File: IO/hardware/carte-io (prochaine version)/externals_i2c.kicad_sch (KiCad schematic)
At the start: 42 parts, among them J10 114020164, J11 114020164, J12 114020164, J13 114020164, J14 114020164, J15 114020164, J16 114020164, J17 114020164, J23 114020164, J24 114020164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

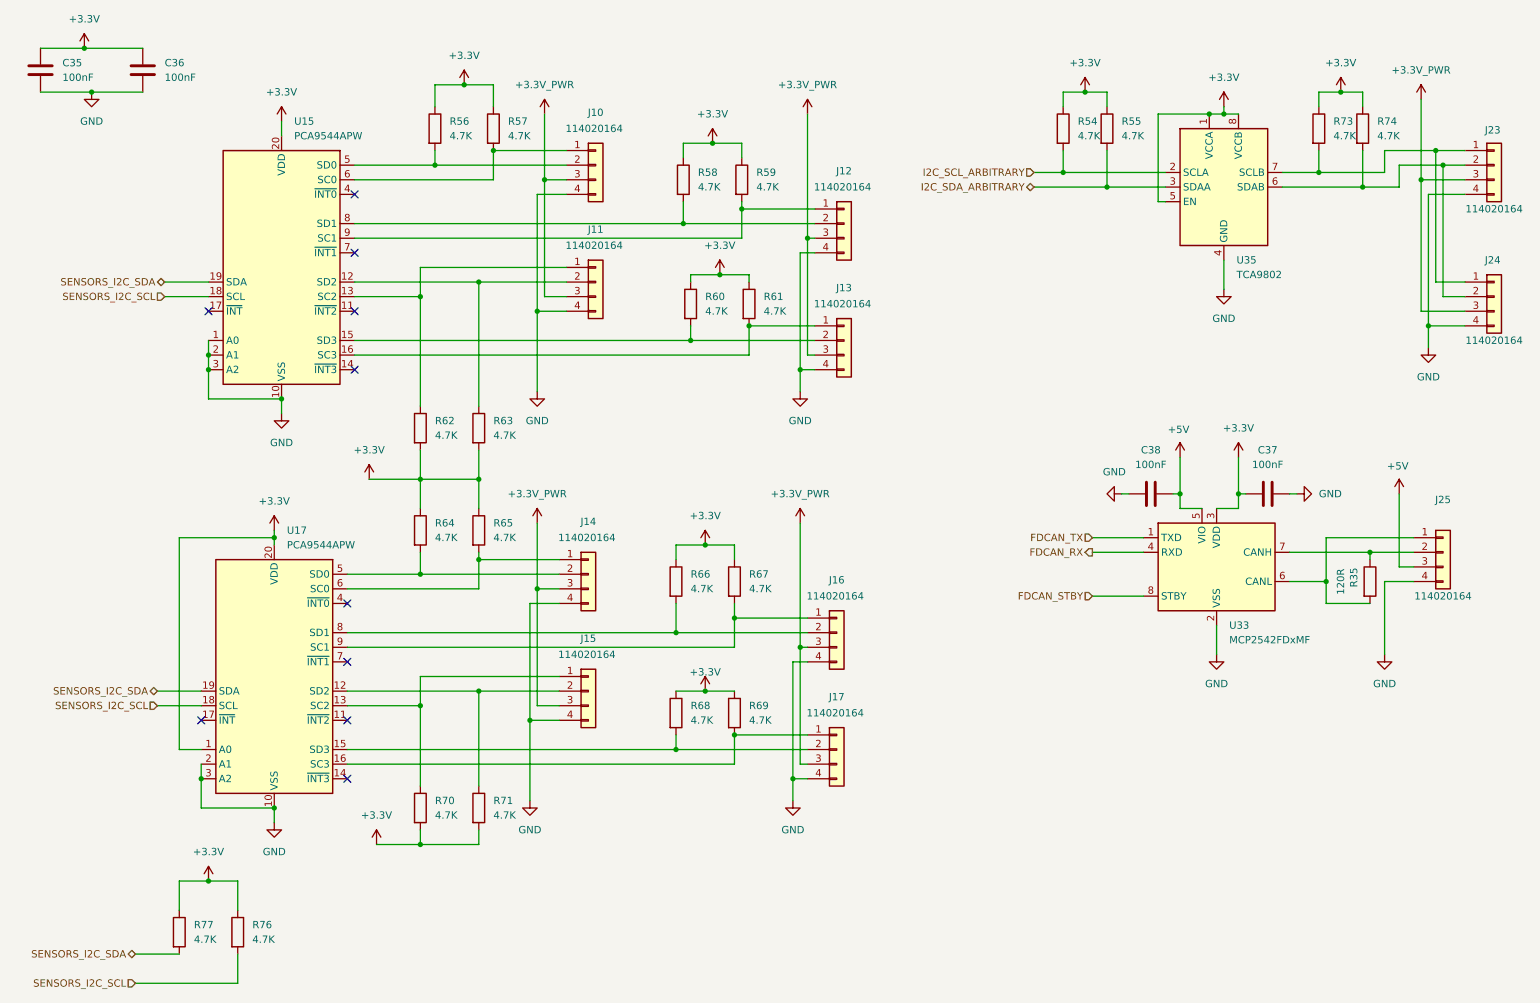
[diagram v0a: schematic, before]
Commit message: Recuperation de la carte IO perdue lors de la suppression des 3 derniers commit
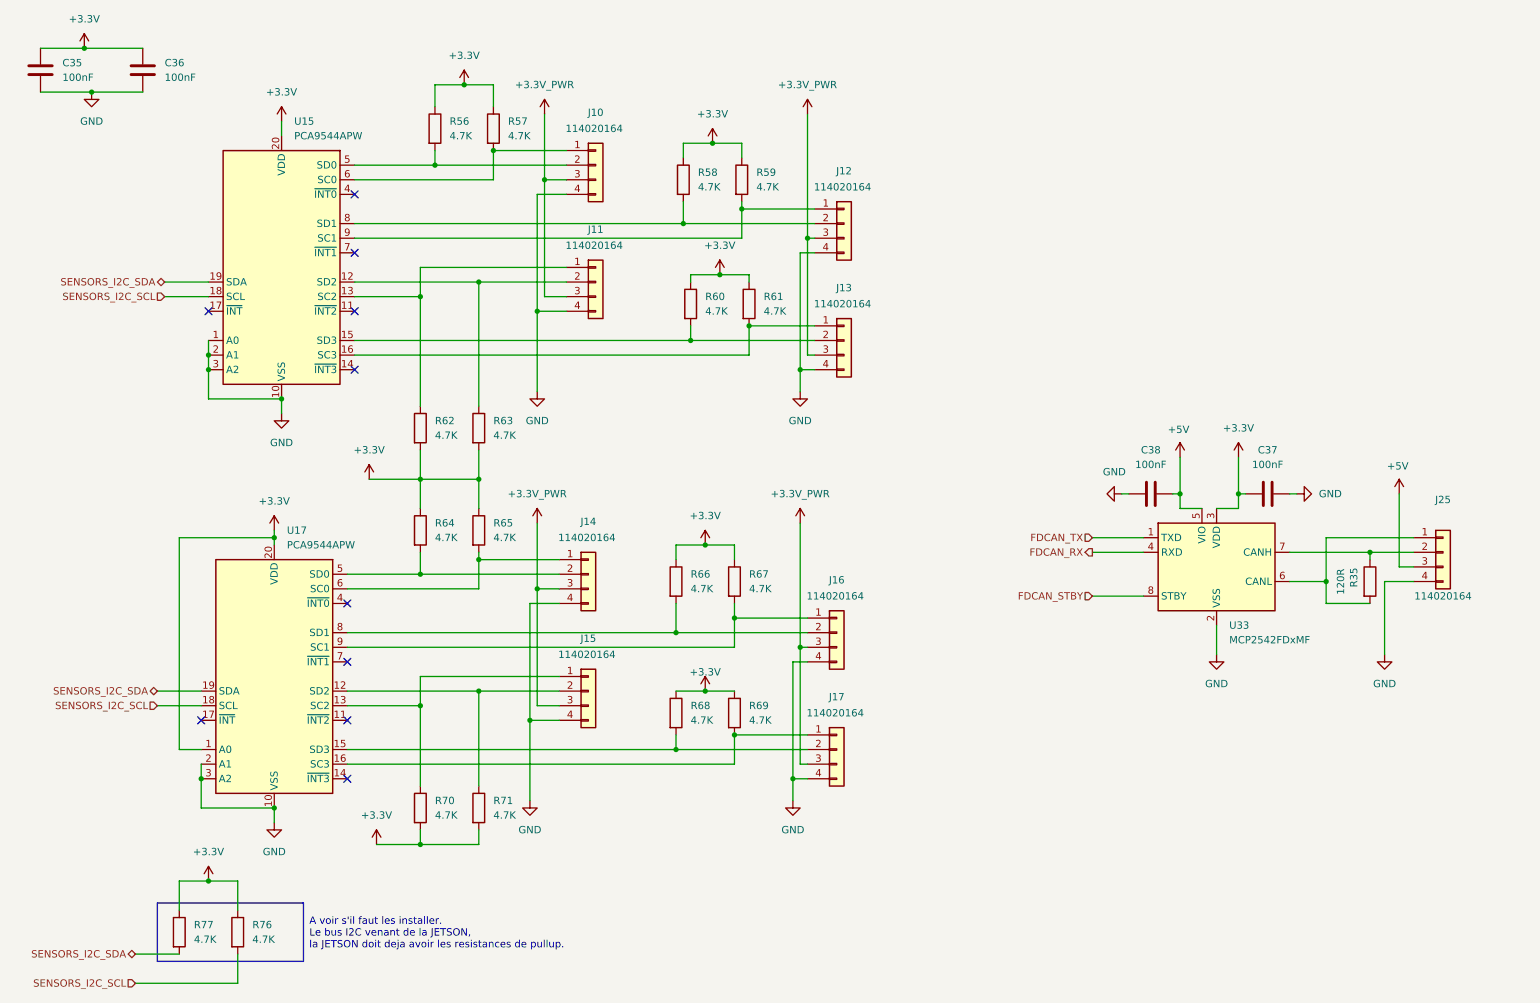
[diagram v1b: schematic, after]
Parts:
- removed J23, J24: 114020164, SeeedStudio - Horizontal Header -114020164:SEEEDSTUDIO_114020164, symbol SeeedStudio - Horizontal header:SeeedStudio - 114020164 - R/A
- removed R54, R55, R73, R74: 4.7K, Resistor_SMD:R_0805_2012Metric_Pad1.20x1.40mm_HandSolder, symbol Device:R
- removed U35: TCA9802, Package_SO:VSSOP-8_3x3mm_P0.65mm, symbol Interface:TCA9802
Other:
- note added: "A voir s'il faut les installer. Le bus I2C venant de la JETSON, la JETSON doit deja avoir les resistances de pullup."
